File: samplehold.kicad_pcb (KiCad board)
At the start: 2 copper layers, 109 x 200 mm, 110 parts, among them J1 in_1, J10 Synth_power_2x5, J2 out_1, J3 trig_1, J4 in_2, J5 out_2, J6 trig_2, J7 in_3, J8 out_3, J9 trig_3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

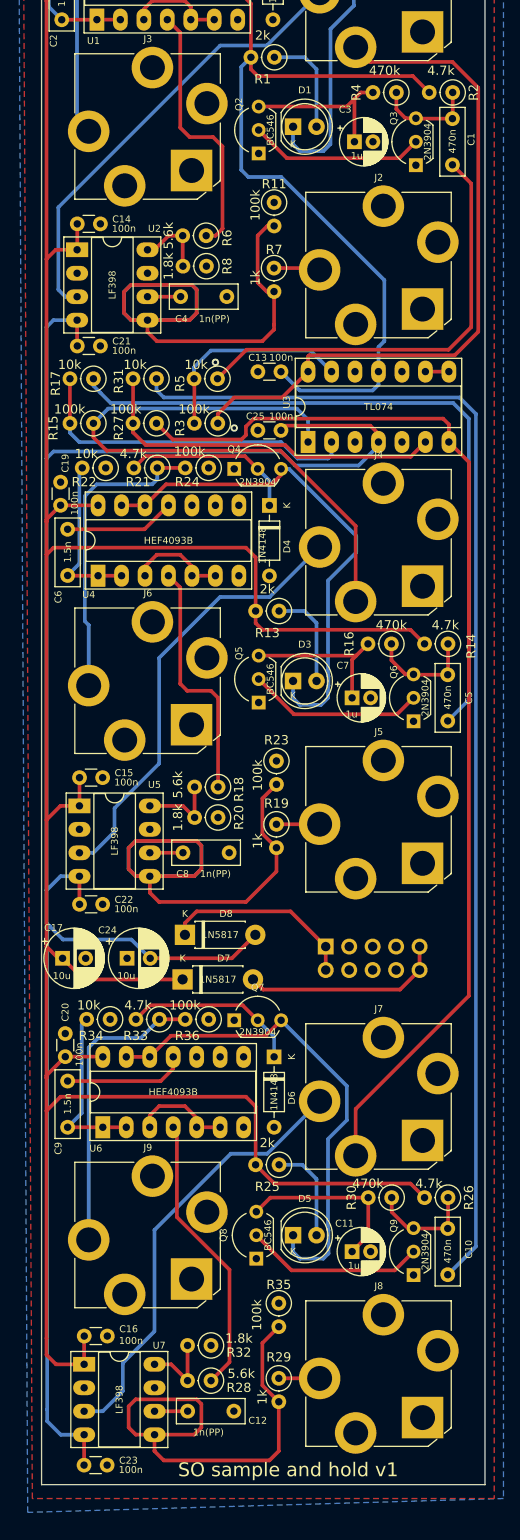
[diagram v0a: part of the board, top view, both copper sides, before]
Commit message: update to 1.1 with 100nF caps instead of 1nF
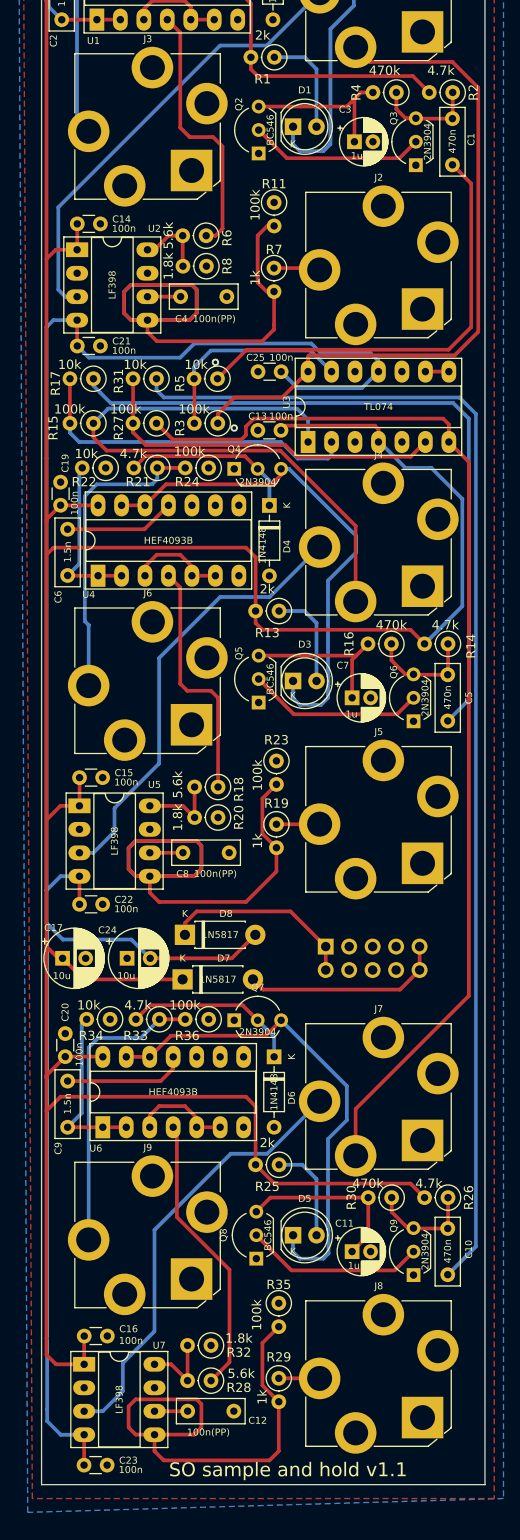
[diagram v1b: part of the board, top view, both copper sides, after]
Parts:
- C12, C4, C8: value 1n(PP) -> 100n(PP)
- moved C25 6.35 mm to (104.4, 96.5)
- moved C13 6.35 mm to (104.4, 102.9)
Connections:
- U3 pad 11: +12V -> -12V
- U3 pad 4: -12V -> +12V
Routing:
- net +12V: track 414.4 -> 399.5 mm
- net -12V: track 215.2 -> 212.7 mm
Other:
- board text added: "SO sample and hold v1.1"
- board text removed: "SO sample and hold v1"
